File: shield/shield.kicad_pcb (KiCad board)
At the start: 2 copper layers, 19.8 x 55.4 mm, 9 parts

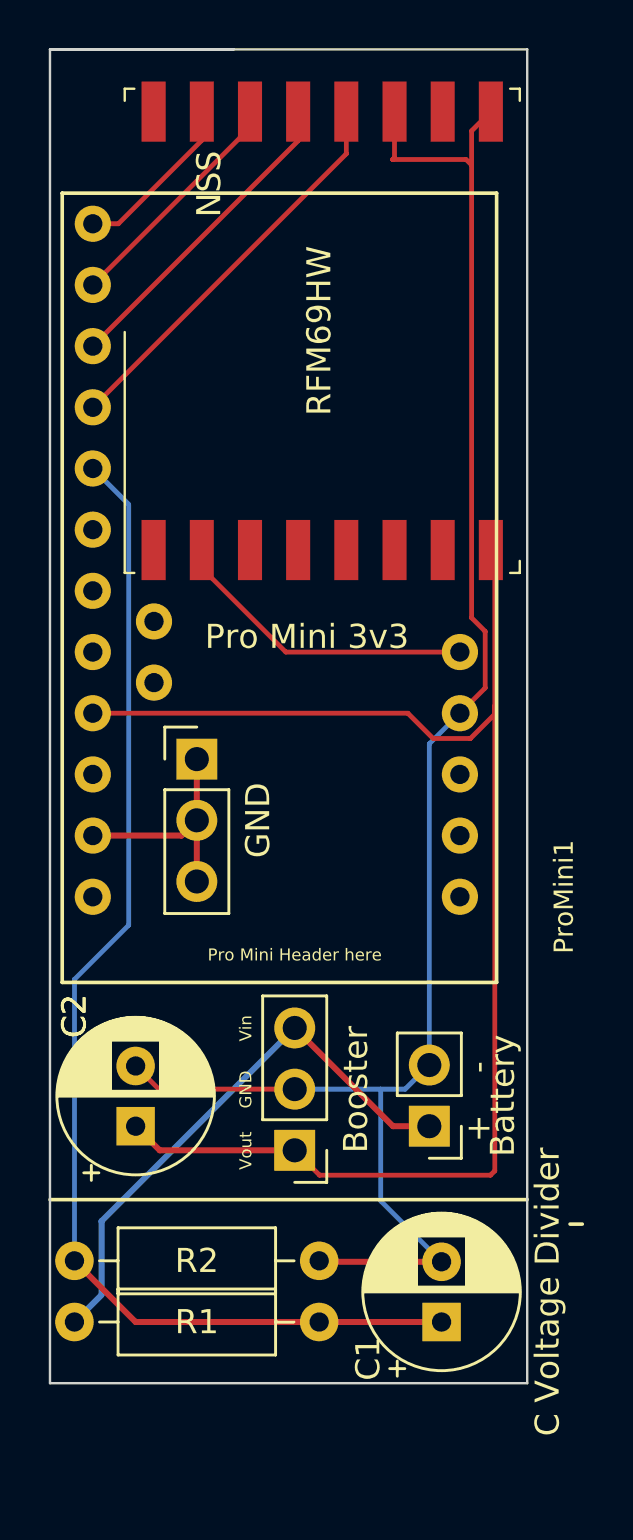
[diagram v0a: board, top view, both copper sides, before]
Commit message: connected Vout
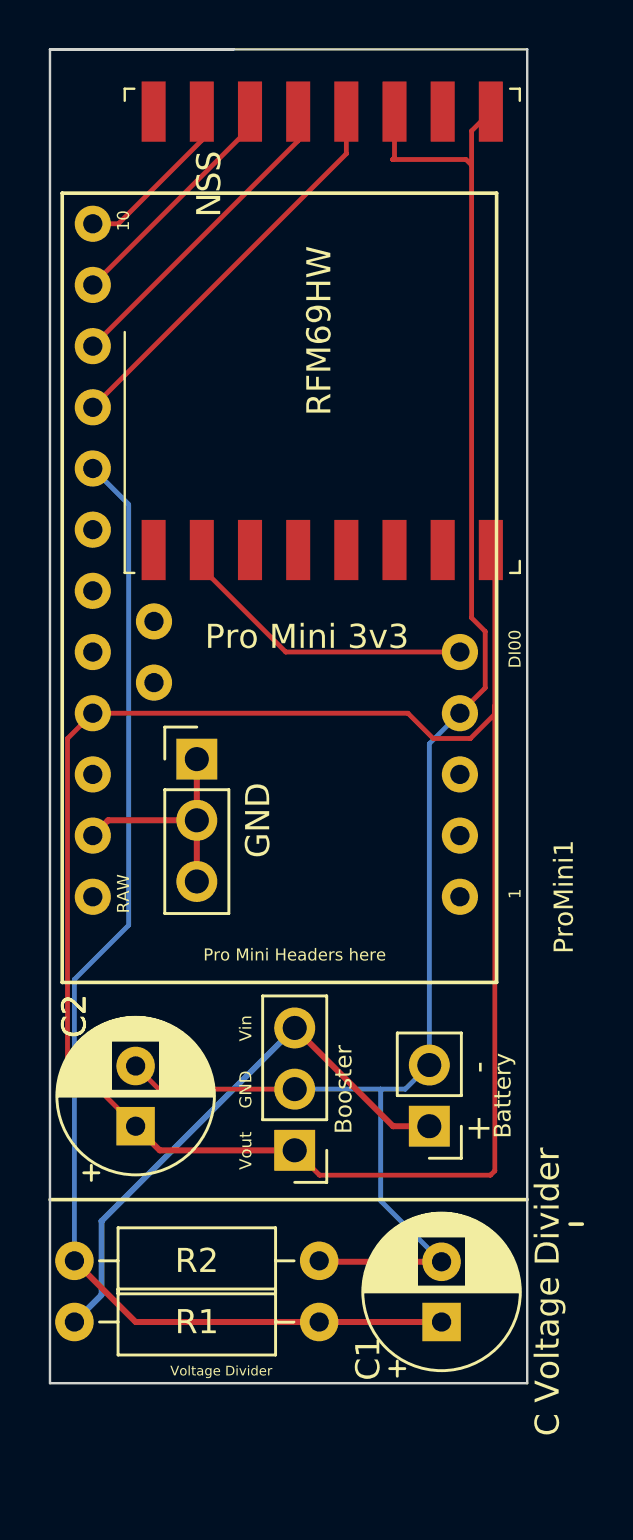
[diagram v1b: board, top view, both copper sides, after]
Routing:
- net Net-(C2-Pad1): track 59.6 -> 78.3 mm
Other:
- board text added: "1"
- board text added: "10"
- board text added: "DI00"
- board text added: "Pro Mini Headers here"
- board text added: "RAW"
- board text added: "Voltage Divider"
- board text removed: "Pro Mini Header here"
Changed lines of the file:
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@@
     (aux_axis_origin 137.16 114.3)
     (pcbplotparams
-      (layerselection 0x0000030_80000001)
+      (layerselection 0x00010f0_ffffffff)
       (disableapertmacros false)
       (usegerberextensions false)
@@
       (outputformat 1)
       (mirror false)
-      (drillshape 1)
+      (drillshape 0)
       (scaleselection 1)
-      (outputdirectory "")
+      (outputdirectory "gerber/")
     )
   )
@@
     (property "Sheetname" "")
     (attr through_hole)
-    (fp_text reference "Booster" (at -2.54 2.525 90) (layer "F.SilkS")
-      (effects (font (size 1 1) (thickness 0.15)))
+    (fp_text reference "Booster" (at -2.032 2.525 90) (layer "F.SilkS")
+      (effects (font (size 0.7 0.7) (thickness 0.15)))
     )
     (fp_text value "Booster Pins" (at 0 6.14) (layer "F.Fab")
@@
     (attr through_hole)
     (fp_text reference "Battery" (at -3.048 1.27 90) (layer "F.SilkS")
-      (effects (font (size 1 1) (thickness 0.15)))
+      (effects (font (size 0.7 0.7) (thickness 0.15)))
     )
     (fp_text value "Battery" (at 0 4.87) (layer "F.Fab")
@@
   (gr_line (start 113.284 54.356) (end 113.284 109.728) (layer "Edge.Cuts") (width 0.1))
   (gr_line (start 113.284 109.728) (end 93.472 109.728) (layer "Edge.Cuts") (width 0.1))
-  (gr_text "Pro Mini Header here" (at 103.632 91.948) (layer "F.SilkS")
+  (gr_text "Pro Mini Headers here" (at 103.632 91.948) (layer "F.SilkS")
     (effects (font (size 0.5 0.5) (thickness 0.125)))
   )
@@
     (effects (font (size 0.5 0.5) (thickness 0.125)))
   )
+  (gr_text "DI00" (at 112.776 79.248 90) (layer "F.SilkS")
+    (effects (font (size 0.5 0.5) (thickness 0.125)))
+  )
+  (gr_text "1" (at 112.776 89.408 90) (layer "F.SilkS")
+    (effects (font (size 0.5 0.5) (thickness 0.125)))
+  )
   (gr_text "+" (at 111.252 99.147621 90) (layer "F.SilkS")
     (effects (font (size 1 1) (thickness 0.15)))
   )
+  (gr_text "10" (at 96.52 61.468 90) (layer "F.SilkS")
+    (effects (font (size 0.5 0.5) (thickness 0.125)))
+  )
   (gr_text "Vin" (at 101.6 94.996 90) (layer "F.SilkS")
     (effects (font (size 0.5 0.5) (thickness 0.125)))
   )
+  (gr_text "RAW" (at 96.52 89.408 90) (layer "F.SilkS")
+    (effects (font (size 0.5 0.5) (thickness 0.125)))
+  )
   (gr_text "-" (at 111.252 96.607621 90) (layer "F.SilkS")
     (effects (font (size 1 1) (thickness 0.15)))
@@
   (gr_text "Vout" (at 101.6 100.076 90) (layer "F.SilkS")
     (effects (font (size 0.5 0.5) (thickness 0.125)))
+  )
+  (gr_text "Voltage Divider" (at 100.584 109.22) (layer "F.SilkS")
+    (effects (font (size 0.4 0.4) (thickness 0.1)))
   )
   (gr_text "NSS" (at 100.076 59.944 90) (layer "F.SilkS")
@@
   (segment (start 103.632 100.061) (end 98.029 100.061) (width 0.25) (layer "F.Cu") (net 1))
   (segment (start 111.939601 81.608399) (end 111.939601 100.912399) (width 0.2) (layer "F.Cu") (net 1))
+  (segment (start 94.199919 96.231919) (end 97.028 99.06) (width 0.2) (layer "F.Cu") (net 1))
   (segment (start 111.775 75.14) (end 111.939601 75.304601) (width 0.2) (layer "F.Cu") (net 1))
   (segment (start 111.939601 100.912399) (end 111.76 101.092) (width 0.2) (layer "F.Cu") (net 1))
+  (segment (start 95.25 81.915) (end 94.199919 82.965081) (width 0.2) (layer "F.Cu") (net 1))
   (segment (start 111.939601 81.608399) (end 111.939601 81.950439) (width 0.2) (layer "F.Cu") (net 1))
   (segment (start 104.663 101.092) (end 103.632 100.061) (width 0.2) (layer "F.Cu") (net 1))
   (segment (start 108.331 81.915) (end 95.25 81.915) (width 0.2) (layer "F.Cu") (net 1))
+  (segment (start 94.199919 82.965081) (end 94.199919 96.231919) (width 0.2) (layer "F.Cu") (net 1))
   (segment (start 111.76 101.092) (end 104.663 101.092) (width 0.2) (layer "F.Cu") (net 1))
   (segment (start 109.381081 82.965081) (end 108.331 81.915) (width 0.2) (layer "F.Cu") (net 1))
@@
   (segment (start 95.612511 106.063489) (end 94.488 107.188) (width 0.25) (layer "B.Cu") (net 4))
   (segment (start 99.187 85.979) (end 99.568 86.36) (width 0.25) (layer "F.Cu") (net 20))
-  (segment (start 95.25 86.995) (end 98.933 86.995) (width 0.25) (layer "F.Cu") (net 20))
+  (segment (start 95.885 86.36) (end 95.25 86.995) (width 0.25) (layer "F.Cu") (net 20))
+  (segment (start 99.568 86.36) (end 95.885 86.36) (width 0.25) (layer "F.Cu") (net 20))
   (segment (start 99.568 86.36) (end 99.568 88.9) (width 0.25) (layer "F.Cu") (net 20))
-  (segment (start 98.933 86.995) (end 99.568 86.36) (width 0.25) (layer "F.Cu") (net 20))
   (segment (start 99.568 83.82) (end 99.568 86.36) (width 0.25) (layer "F.Cu") (net 20))
   (segment (start 103.26 79.375) (end 110.49 79.375) (width 0.2) (layer "F.Cu") (net 21))

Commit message: final changes before printing
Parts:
- moved R1 0.51 mm to (94.5, 107.7)
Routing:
- net +3V3: track 23.3 -> 23.8 mm
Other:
- outline, holes or cut-outs redrawn
- board text added: "2"
- board text added: "TX0"
- board text removed: "1"
- board text removed: "DI00"
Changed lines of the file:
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@@
   )
   (footprint "Resistor_THT:R_Axial_DIN0207_L6.3mm_D2.5mm_P10.16mm_Horizontal" (layer "F.Cu")
-    (at 94.488 107.188)
+    (at 94.488 107.696)
     (descr "Resistor, Axial_DIN0207 series, Axial, Horizontal, pin pitch=10.16mm, 0.25W = 1/4W, length*diameter=6.3*2.5mm^2, http://cdn-reichelt.de/documents/datenblatt/B400/1_4W%23YAG.pdf")
     (tags "Resistor Axial_DIN0207 series Axial Horizontal pin pitch 10.16mm 0.25W = 1/4W length 6.3mm diameter 2.5mm")
@@
   (gr_line (start 115.062 103.124) (end 115.57 103.124) (layer "F.SilkS") (width 0.15))
   (gr_line (start 113.284 102.108) (end 93.472 102.108) (layer "F.SilkS") (width 0.15))
-  (gr_line (start 93.472 54.356) (end 101.092 54.356) (layer "Edge.Cuts") (width 0.1))
   (gr_line (start 93.472 54.356) (end 113.284 54.356) (layer "Edge.Cuts") (width 0.1))
   (gr_line (start 93.472 109.728) (end 93.472 54.356) (layer "Edge.Cuts") (width 0.1))
@@
     (effects (font (size 0.5 0.5) (thickness 0.125)))
   )
-  (gr_text "DI00" (at 112.776 79.248 90) (layer "F.SilkS")
-    (effects (font (size 0.5 0.5) (thickness 0.125)))
-  )
-  (gr_text "1" (at 112.776 89.408 90) (layer "F.SilkS")
+  (gr_text "2" (at 112.776 79.248 90) (layer "F.SilkS")
+    (effects (font (size 0.5 0.5) (thickness 0.125)))
+  )
+  (gr_text "TX0" (at 112.776 89.408 90) (layer "F.SilkS")
     (effects (font (size 0.5 0.5) (thickness 0.125)))
   )
@@
     (effects (font (size 0.5 0.5) (thickness 0.125)))
   )
-  (gr_text "Voltage Divider" (at 100.584 109.22) (layer "F.SilkS")
+  (gr_text "Voltage Divider" (at 101.6 102.616) (layer "F.SilkS")
     (effects (font (size 0.4 0.4) (thickness 0.1)))
   )
@@
   (segment (start 110.49 81.915) (end 109.22 83.185) (width 0.2) (layer "B.Cu") (net 2))
   (segment (start 109.22 96.52) (end 108.219 97.521) (width 0.2) (layer "B.Cu") (net 2))
-  (segment (start 104.648 107.188) (end 109.728 107.188) (width 0.25) (layer "F.Cu") (net 3))
-  (segment (start 97.028 107.188) (end 94.488 104.648) (width 0.25) (layer "F.Cu") (net 3))
-  (segment (start 104.648 107.188) (end 97.028 107.188) (width 0.25) (layer "F.Cu") (net 3))
+  (segment (start 97.536 107.696) (end 94.488 104.648) (width 0.25) (layer "F.Cu") (net 3))
+  (segment (start 105.156 107.188) (end 104.648 107.696) (width 0.25) (layer "F.Cu") (net 3))
+  (segment (start 109.728 107.188) (end 105.156 107.188) (width 0.25) (layer "F.Cu") (net 3))
+  (segment (start 104.648 107.696) (end 97.536 107.696) (width 0.25) (layer "F.Cu") (net 3))
   (segment (start 96.739919 90.712081) (end 94.488 92.964) (width 0.2) (layer "B.Cu") (net 3))
   (segment (start 96.739919 73.244919) (end 96.739919 90.712081) (width 0.2) (layer "B.Cu") (net 3))
@@
   (segment (start 109.22 99.06) (end 107.711 99.06) (width 0.25) (layer "F.Cu") (net 4))
   (segment (start 107.711 99.06) (end 103.632 94.981) (width 0.25) (layer "F.Cu") (net 4))
-  (segment (start 95.612511 103.000489) (end 95.612511 106.063489) (width 0.25) (layer "B.Cu") (net 4))
+  (segment (start 95.612511 103.000489) (end 95.612511 106.571489) (width 0.25) (layer "B.Cu") (net 4))
   (segment (start 103.632 94.981) (end 95.612511 103.000489) (width 0.25) (layer "B.Cu") (net 4))
-  (segment (start 95.612511 106.063489) (end 94.488 107.188) (width 0.25) (layer "B.Cu") (net 4))
+  (segment (start 95.612511 106.571489) (end 94.488 107.696) (width 0.25) (layer "B.Cu") (net 4))
   (segment (start 99.187 85.979) (end 99.568 86.36) (width 0.25) (layer "F.Cu") (net 20))
   (segment (start 95.885 86.36) (end 95.25 86.995) (width 0.25) (layer "F.Cu") (net 20))
